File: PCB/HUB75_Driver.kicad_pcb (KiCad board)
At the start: 2 copper layers, 48.3 x 53.3 mm, 15 parts, among them U1 ESP32_DevKit_V1_DOIT

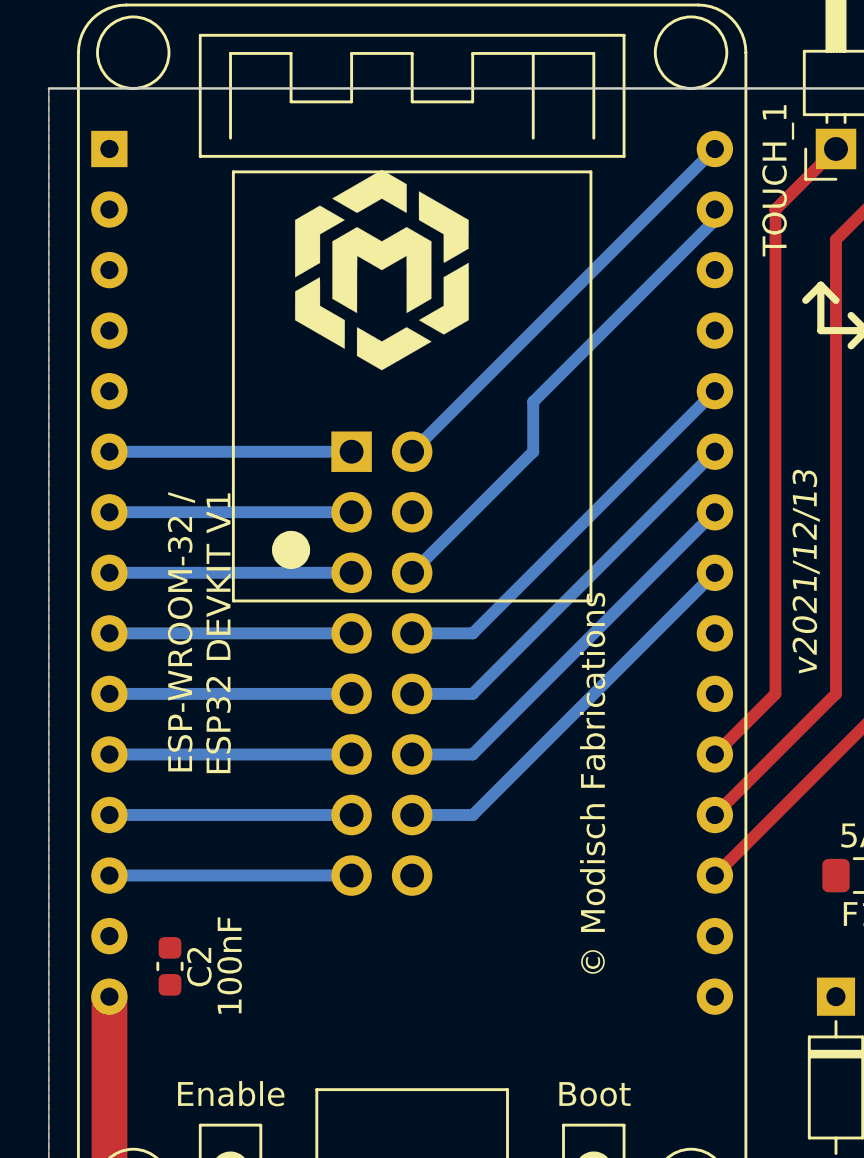
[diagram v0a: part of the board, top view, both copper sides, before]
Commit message: fix missing wires, use blue PCB
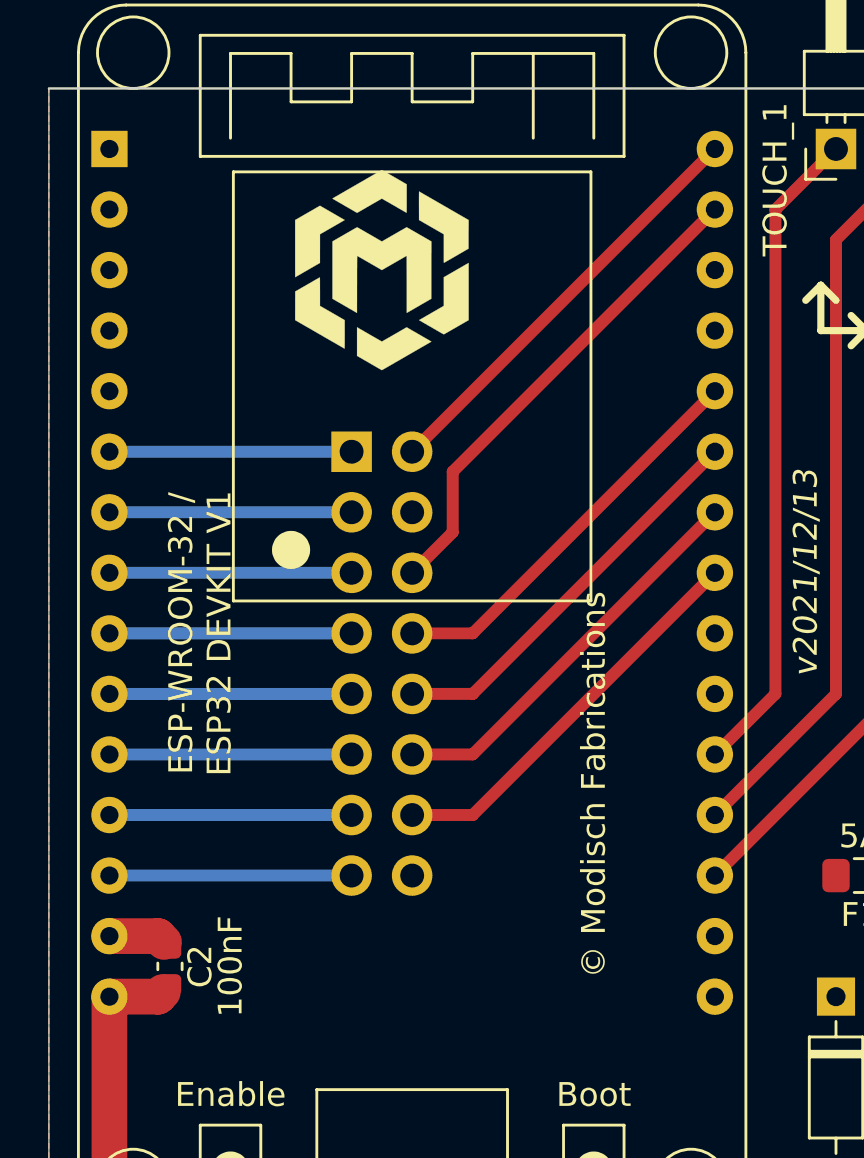
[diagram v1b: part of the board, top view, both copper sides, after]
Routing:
- net GND: track 0.00 -> 2.39 mm
- net Net-(C2-Pad1): track 12.7 -> 15.0 mm

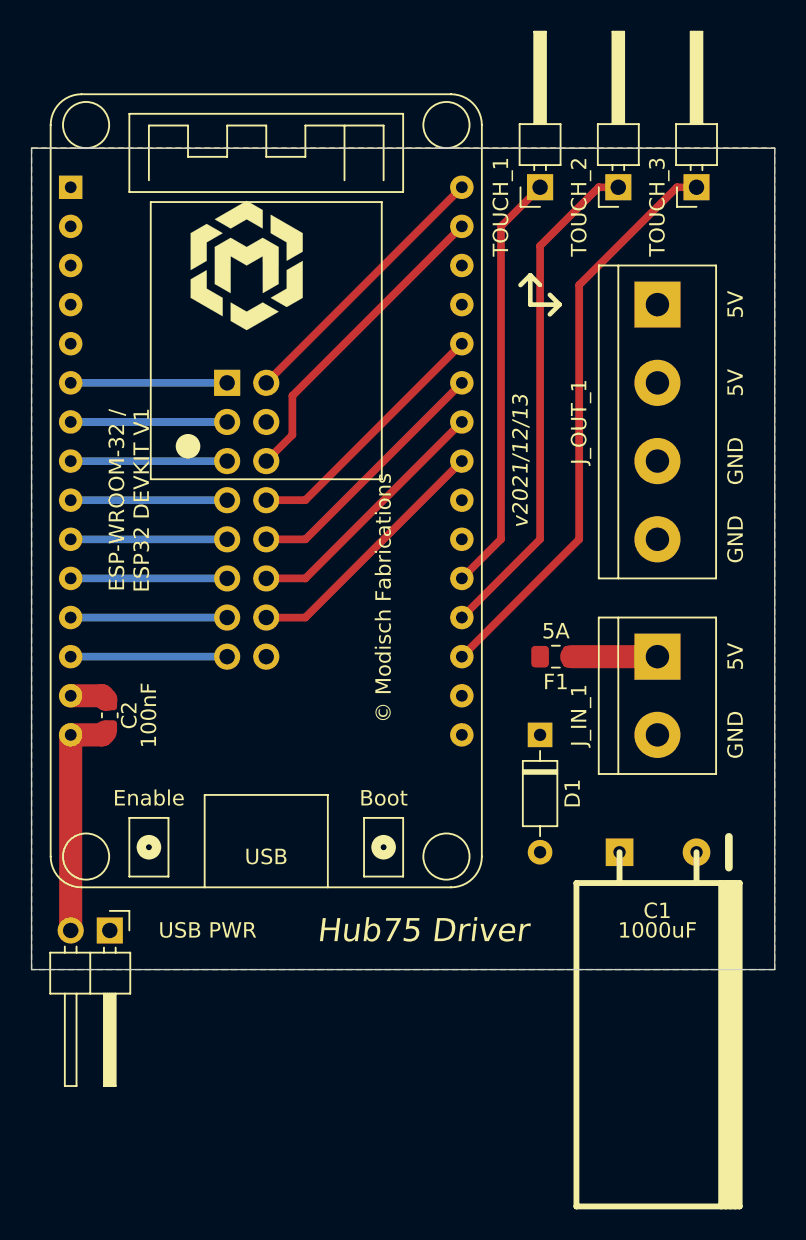
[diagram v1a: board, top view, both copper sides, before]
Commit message: add reset capacitor
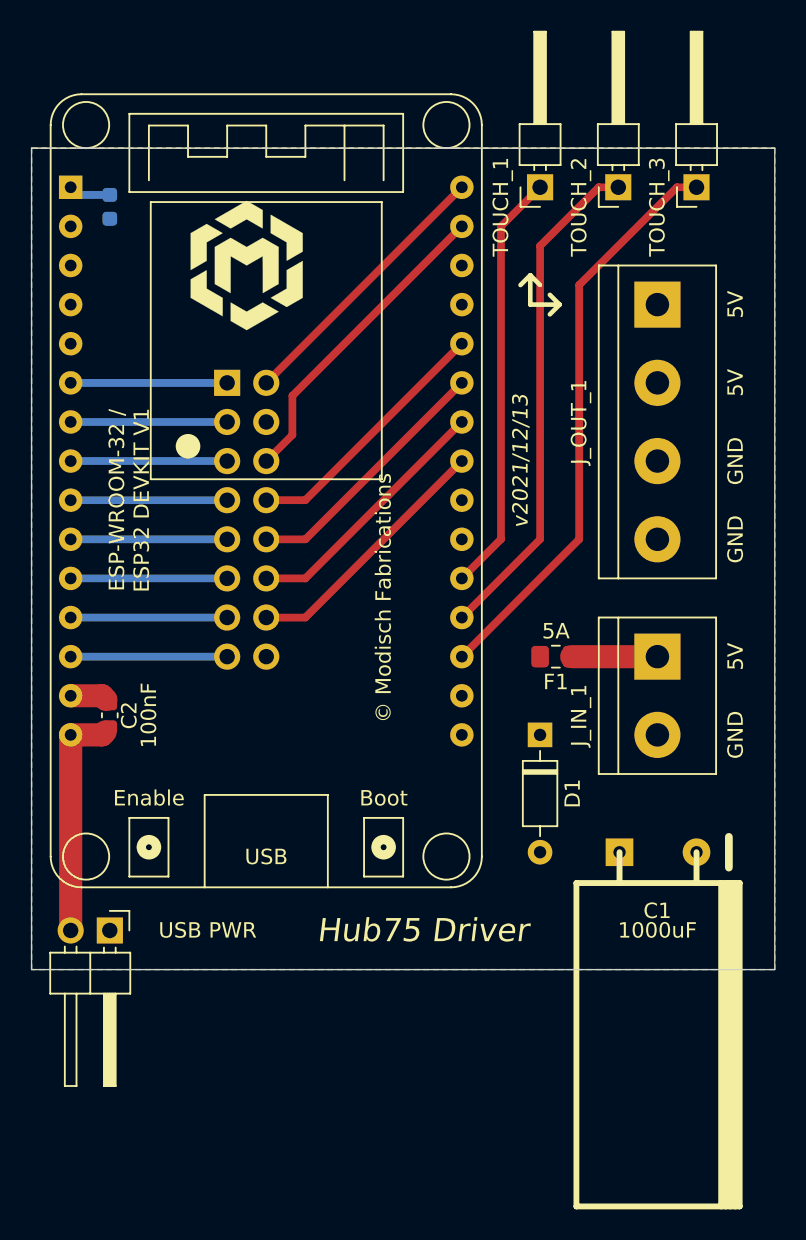
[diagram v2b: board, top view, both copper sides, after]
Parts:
- added C_PROG_1: 10uF, Capacitor_SMD:C_0603_1608Metric, B.Cu at (213.4, 29.2)
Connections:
- U1 pad 1: (no net) -> Net-(C_PROG_1-Pad1)
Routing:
- net Net-(C_PROG_1-Pad1): track 0.00 -> 2.75 mm
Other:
- board text added: "*RESET"
